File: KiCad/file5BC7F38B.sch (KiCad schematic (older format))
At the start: 72 parts, among them J301 DB9_Female, P301 ISP/PDI, P302 Thru, P304 Header, Q301 PN2222A, SW301 SPST, U301 DS3231, U302 ATmega1284P-AU, U303 LP2992, U304 SI5351A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

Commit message: Design Updates
Updating schematic parts
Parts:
- C303, C304, C313, C314, C315, C317, C318: footprint Capacitors_SMD:C_0805_HandSoldering -> Capacitors_SMD:C_0805
- R308, R313: footprint Resistors_SMD:R_0805_HandSoldering -> Resistors_SMD:R_0805
- SJ301: footprint (none) -> Wire_Connections_Bridges:Solder-Jumper-NO-SMD-Pad_Small; Digi-Key Part No. (none) -> np; Link (none) -> np; Manufacturer (none) -> np
- TP301: footprint (none) -> Pin_Headers:Pin_Header_Straight_1x03
- TP302: footprint (none) -> Pin_Headers:Pin_Header_Straight_1x04
- U304: footprint Housings_SSOP:MSOP-10_3x3mm_Pitch0.5mm_Handsolder -> Housings_SSOP:MSOP-10_3x3mm_Pitch0.5mm
- U307: footprint Housings_SSOP:TSSOP-8_3x3mm_Pitch0.65mm_Handsolder -> Housings_SSOP:TSSOP-8_3x3mm_Pitch0.65mm
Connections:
- net labels removed: CLK0, CLK2, PB5
- wire segments 298 -> 297
- no-connect marks 16 -> 19
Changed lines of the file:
@@
 F 0 "U304" H 11850 3650 60  0000 C CNB
 F 1 "SI5351A" H 11850 3150 60  0000 C CNB
-F 2 "Housings_SSOP:MSOP-10_3x3mm_Pitch0.5mm_Handsolder" H 11850 3150 50  0001 C CNN
+F 2 "Housings_SSOP:MSOP-10_3x3mm_Pitch0.5mm" H 11850 3150 50  0001 C CNN
 F 3 "http://www.silabs.com/Support%20Documents/TechnicalDocs/Si5351-B.pdf" H 11850 3150 50  0001 C CNN
 F 4 "336-2399-5-ND" H 11850 3150 50  0001 C CNN "Digi-Key Part No."
@@
 F 0 "C304" H 5500 4900 50  0000 L CNN
 F 1 "10uF" H 5550 5050 50  0000 L CNN
-F 2 "Capacitors_SMD:C_0805_HandSoldering" H 5450 5000 50  0001 C CNN
+F 2 "Capacitors_SMD:C_0805" H 5450 5000 50  0001 C CNN
 F 3 "" H 5450 5000 50  0001 C CNN
 F 4 "490-5523-1-ND" H 5450 5000 50  0001 C CNN "Digi-Key Part No."
@@
 	-1   0    0    1
 $EndComp
-Text Label 4350 5600 0    39   ~ 0
-PB3
-Text Label 3850 5500 2    39   ~ 0
-PB4
-Text Label 3850 5600 2    39   ~ 0
-PB5
 Text Notes 10750 2300 0    79   ~ 16
 SI5351 Clock
@@
 Connection ~ 10550 4350
 Wire Wire Line
-	12500 2250 12500 2950
-Wire Wire Line
 	12600 2250 12600 3050
 $Comp
@@
 Text GLabel 12600 2250 1    39   Output ~ 0
 CLK1
-Text GLabel 12500 2250 1    39   Output ~ 0
-CLK0
 Text GLabel 7950 6550 2    39   Output ~ 0
 HF_ENABLE
@@
 F 0 "U307" H 10200 4500 61  0000 C CNB
 F 1 "SN74CB3Q3305" H 10450 4000 61  0000 C CNB
-F 2 "Housings_SSOP:TSSOP-8_3x3mm_Pitch0.65mm_Handsolder" H 10050 3850 50  0001 C CNN
+F 2 "Housings_SSOP:TSSOP-8_3x3mm_Pitch0.65mm" H 10050 3850 50  0001 C CNN
 F 3 "" H 10050 4300 50  0001 C CNN
 F 4 "296-16809-1-ND" H 10050 4250 50  0001 C CNN "Digi-Key Part No."
@@
 	8250 3650 8250 3700
 Connection ~ 8250 3700
-Text GLabel 12500 3350 2    39   Output ~ 0
-CLK2
 Wire Wire Line
 	4450 3500 4450 3850
@@
 F 0 "TP302" V 9550 3650 50  0000 L CNN
 F 1 "I2C0" V 9450 3650 50  0000 L CNN
-F 2 "" H 9350 3800 50  0001 C CNN
+F 2 "Pin_Headers:Pin_Header_Straight_1x04" H 9350 3800 50  0001 C CNN
 F 3 "" H 9350 3800 50  0001 C CNN
 F 4 "np" H 9350 3800 50  0001 C CNN "Digi-Key Part No."
@@
 F 0 "TP301" V 10750 3700 50  0000 L CNN
 F 1 "I2C1" V 10650 3700 50  0000 L CNN
-F 2 "" H 10550 3800 50  0001 C CNN
+F 2 "Pin_Headers:Pin_Header_Straight_1x03" H 10550 3800 50  0001 C CNN
 F 3 "" H 10550 3800 50  0001 C CNN
 F 4 "np" H 10550 3800 50  0001 C CNN "Digi-Key Part No."
@@
 F 0 "R313" V 2630 9700 50  0000 C CNN
 F 1 "100k" V 2550 9700 50  0000 C CNN
-F 2 "Resistors_SMD:R_0805_HandSoldering" H 2480 9700 50  0001 C CNN
+F 2 "Resistors_SMD:R_0805" H 2480 9700 50  0001 C CNN
 F 3 "" H 2550 9700 50  0001 C CNN
 F 4 "311-100KCRCT-ND" H 2550 9700 50  0001 C CNN "Digi-Key Part No."
@@
 F 0 "SJ301" H 2950 7100 50  0000 C CNN
 F 1 "SolderJumper_2_Open" H 2950 7114 50  0001 C CNN
-F 2 "" H 2950 7000 50  0001 C CNN
+F 2 "Wire_Connections_Bridges:Solder-Jumper-NO-SMD-Pad_Small" H 2950 7000 50  0001 C CNN
 F 3 "" H 2950 7000 50  0001 C CNN
+F 4 "np" H 2950 7000 50  0001 C CNN "Digi-Key Part No."
+F 5 "np" H 2950 7000 50  0001 C CNN "Link"
+F 6 "np" H 2950 7000 50  0001 C CNN "Manufacturer"
 	1    2950 7000
 	0    -1   -1   0
@@
 F 0 "C303" H 2200 2150 50  0000 L CNN
 F 1 "4.7uF" H 2475 2150 50  0000 L CNN
-F 2 "Capacitors_SMD:C_0805_HandSoldering" H 2488 2100 50  0001 C CNN
+F 2 "Capacitors_SMD:C_0805" H 2488 2100 50  0001 C CNN
 F 3 "" H 2450 2250 50  0001 C CNN
 F 4 "587-2990-1-ND" H 2450 2250 50  0001 C CNN "Digi-Key Part No."
@@
 F 8 "IC REG LINEAR 3.3V 250MA SOT23-5" H 14750 6800 50  0001 C CNN "Description"
 	1    14750 6800
-	1    0    0    -1
+	-1   0    0    -1
 $EndComp
 $Comp
@@
 F 0 "C318" H 3650 2150 50  0000 L CNN
 F 1 "4.7uF" H 3925 2150 50  0000 L CNN
-F 2 "Capacitors_SMD:C_0805_HandSoldering" H 3938 2100 50  0001 C CNN
+F 2 "Capacitors_SMD:C_0805" H 3938 2100 50  0001 C CNN
 F 3 "" H 3900 2250 50  0001 C CNN
 F 4 "587-2990-1-ND" H 3900 2250 50  0001 C CNN "Digi-Key Part No."
@@
 F 0 "C317" H 3650 3550 50  0000 L CNN
 F 1 "4.7uF" H 3925 3550 50  0000 L CNN
-F 2 "Capacitors_SMD:C_0805_HandSoldering" H 3938 3500 50  0001 C CNN
+F 2 "Capacitors_SMD:C_0805" H 3938 3500 50  0001 C CNN
 F 3 "" H 3900 3650 50  0001 C CNN
 F 4 "587-2990-1-ND" H 3900 3650 50  0001 C CNN "Digi-Key Part No."
@@
 F 0 "C314" H 2200 3550 50  0000 L CNN
 F 1 "4.7uF" H 2475 3550 50  0000 L CNN
-F 2 "Capacitors_SMD:C_0805_HandSoldering" H 2488 3500 50  0001 C CNN
+F 2 "Capacitors_SMD:C_0805" H 2488 3500 50  0001 C CNN
 F 3 "" H 2450 3650 50  0001 C CNN
 F 4 "587-2990-1-ND" H 2450 3650 50  0001 C CNN "Digi-Key Part No."
@@
 F 0 "C313" H 13750 6850 50  0000 L CNN
 F 1 "4.7uF" H 14025 6850 50  0000 L CNN
-F 2 "Capacitors_SMD:C_0805_HandSoldering" H 14038 6800 50  0001 C CNN
+F 2 "Capacitors_SMD:C_0805" H 14038 6800 50  0001 C CNN
 F 3 "" H 14000 6950 50  0001 C CNN
 F 4 "587-2990-1-ND" H 14000 6950 50  0001 C CNN "Digi-Key Part No."
@@
 F 0 "C315" H 15200 6850 50  0000 L CNN
 F 1 "4.7uF" H 15475 6850 50  0000 L CNN
-F 2 "Capacitors_SMD:C_0805_HandSoldering" H 15488 6800 50  0001 C CNN
+F 2 "Capacitors_SMD:C_0805" H 15488 6800 50  0001 C CNN
 F 3 "" H 15450 6950 50  0001 C CNN
 F 4 "587-2990-1-ND" H 15450 6950 50  0001 C CNN "Digi-Key Part No."
@@
 F 0 "R308" V 2530 7400 50  0000 C CNN
 F 1 "100k" V 2450 7400 50  0000 C CNN
-F 2 "Resistors_SMD:R_0805_HandSoldering" H 2380 7400 50  0001 C CNN
+F 2 "Resistors_SMD:R_0805" H 2380 7400 50  0001 C CNN
 F 3 "" H 2450 7400 50  0001 C CNN
 F 4 "311-100KCRCT-ND" H 2450 7400 50  0001 C CNN "Digi-Key Part No."
@@
 	1    0    0    -1
 $EndComp
+Text Label 7800 3450 0    39   ~ 0
+PA0
+Text Label 7800 3550 0    39   ~ 0
+PA1
+NoConn ~ 12500 2950
+NoConn ~ 12500 3350
+NoConn ~ 8250 6750
 Wire Bus Line
 	7700 3250 7700 7050

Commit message: Design Updates
Updated schematics parts descriptions
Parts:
- D306, D307: symbol Diode:ESD9B5.0ST5G -> Power_Protection:TVS_Diode
- P301: symbol FlexFox80-rescue:CONN_02X03-ARDF-2-Band-MiniTx-rescue -> Connector:ISP_PDI
- U303, U306, U308: symbol FlexFox80-rescue:MIC5219-ARDF-2-Band-MiniTx-rescue -> Regulator_Linear:LP2992
- U307: symbol FlexFox80-rescue:SN74CB3Q3305-ARDF-2-Band-MiniTx-rescue -> Interface:SN74CB3Q3305
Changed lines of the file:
@@
 ~RESET~
 $Comp
-L FlexFox80-rescue:CONN_02X03-ARDF-2-Band-MiniTx-rescue P301
+L Connector:ISP_PDI P301
 U 1 1 57AD5B1A
 P 4100 5600
@@
 F 1 "ISP/PDI" H 4100 5400 50  0000 C CNN
 F 2 "Pin_Headers:SM_Pin_Header_Straight_2x03" H 4100 4400 50  0001 C CNN
-F 3 "http://katalog.we-online.de/em/datasheet/6100xx21121.pdf" H 4100 4400 50  0001 C CNN
+F 3 "" H 4100 4400 50  0001 C CNN
 F 4 "609-3487-1-ND" H 4100 5600 50  0001 C CNN "Digi-Key Part No."
 F 5 "<a href=\"https://www.digikey.com/products/en?keywords=609-3487-1-ND\">Link</a>" H 4100 5600 60  0001 C CNN "Link"
@@
 Connection ~ 10050 3900
 $Comp
-L FlexFox80-rescue:SN74CB3Q3305-ARDF-2-Band-MiniTx-rescue U307
+L Interface:SN74CB3Q3305 U307
 U 1 1 5C75D7C5
 P 10050 4250
@@
 	4200 2050 3900 2050
 $Comp
-L FlexFox80-rescue:MIC5219-ARDF-2-Band-MiniTx-rescue U303
+L Regulator_Linear:LP2992 U303
 U 1 1 60F38BB8
 P 3150 2100
@@
 	1000 8650 1700 8650
 $Comp
-L Diode:ESD9B5.0ST5G D306
+L Power_Protection:TVS_Diode D306
 U 1 1 612F5B15
 P 3750 9800
@@
 $EndComp
 $Comp
-L FlexFox80-rescue:MIC5219-ARDF-2-Band-MiniTx-rescue U308
+L Regulator_Linear:LP2992 U308
 U 1 1 60E1E02E
 P 3200 3550
@@
 $EndComp
 $Comp
-L FlexFox80-rescue:MIC5219-ARDF-2-Band-MiniTx-rescue U306
+L Regulator_Linear:LP2992 U306
 U 1 1 60E3CCEB
 P 14750 6800
@@
 $EndComp
 $Comp
-L Diode:ESD9B5.0ST5G D307
+L Power_Protection:TVS_Diode D307
 U 1 1 609FB9B8
 P 4100 9800

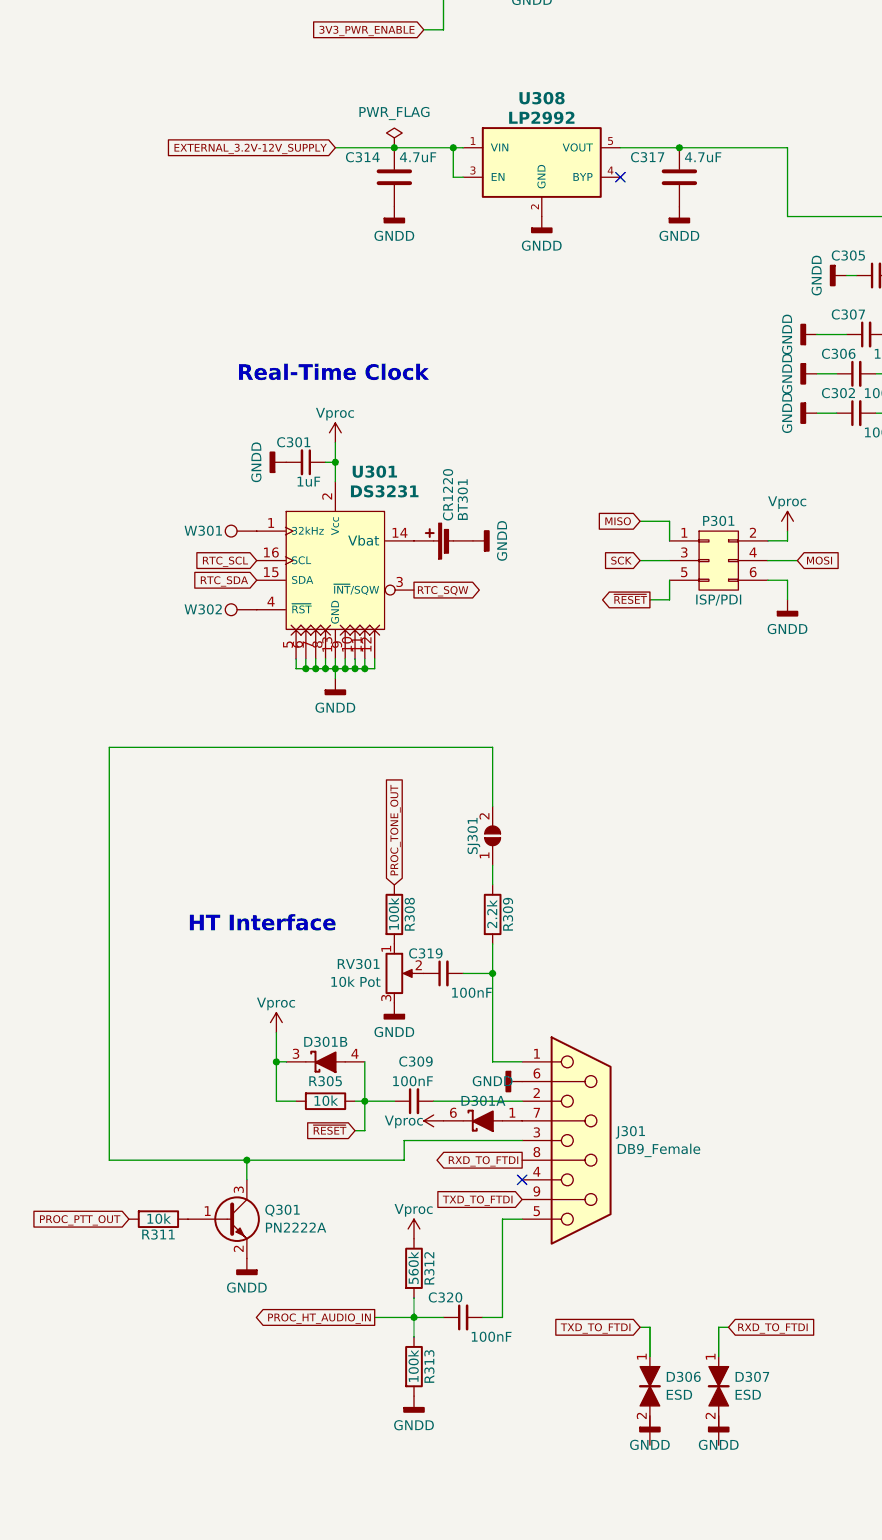
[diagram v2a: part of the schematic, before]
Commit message: PCB Updates
o Started PCB layout
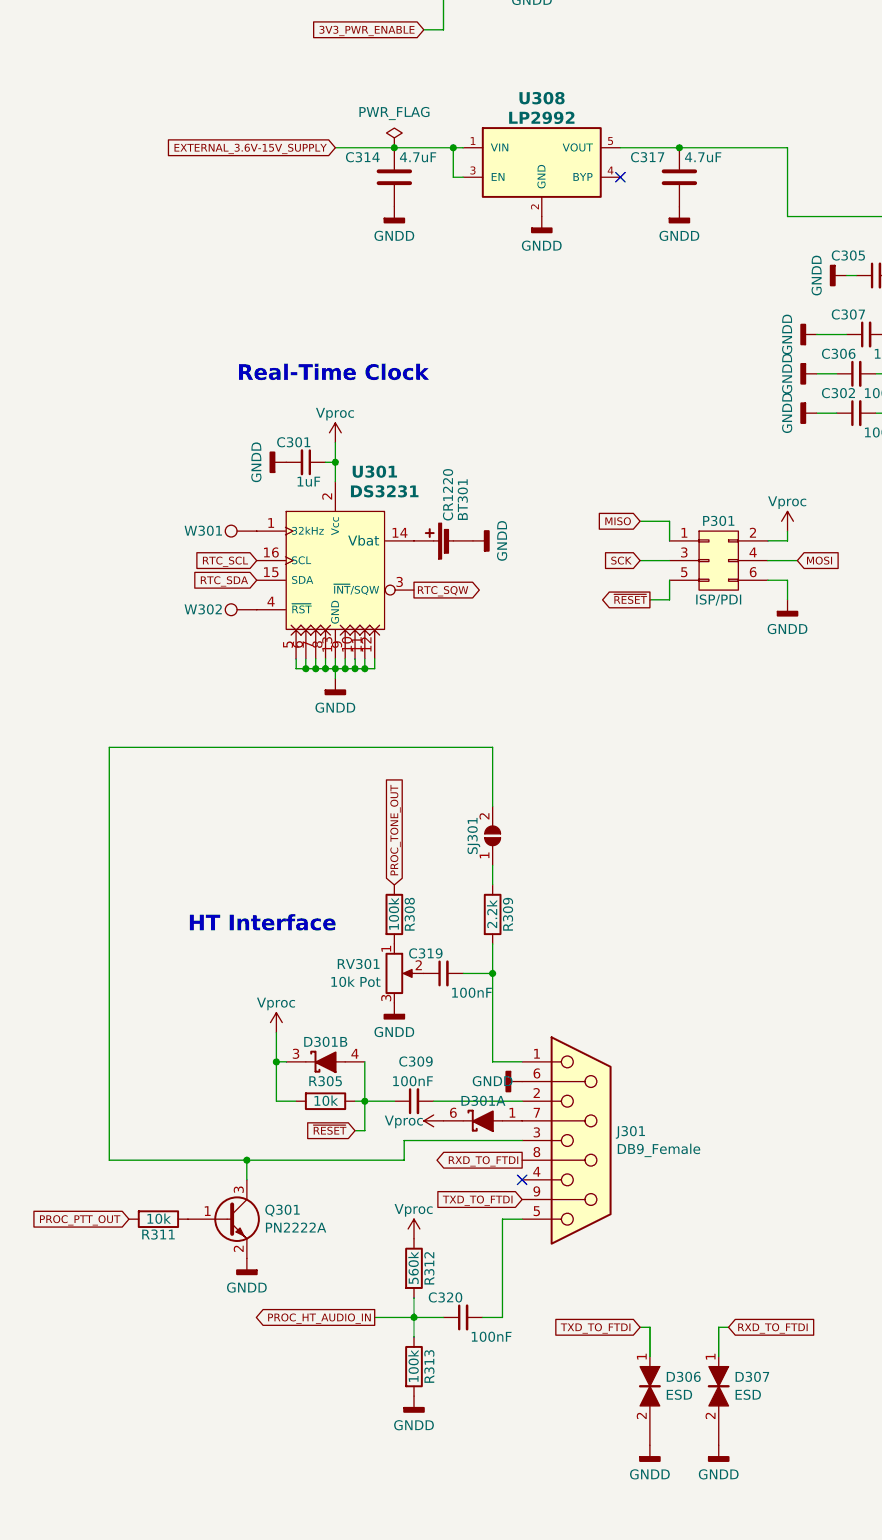
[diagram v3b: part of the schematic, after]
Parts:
- U302: footprint Package_QFP:TQFP-44_10x10mm_P0.8mm -> Housings_QFP:TQFP-44_10x10mm_Pitch0.8mm
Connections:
- net GND: now also D306.2, D307.2
- net EXTERNAL_3.2V-12V_SUPPLY renamed EXTERNAL_3.6V-15V_SUPPLY
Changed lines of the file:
@@
 Connection ~ 2750 3500
 Text GLabel 2150 3500 0    39   Input ~ 0
-EXTERNAL_3.2V-12V_SUPPLY
+EXTERNAL_3.6V-15V_SUPPLY
 NoConn ~ 3600 3650
 NoConn ~ 14350 6900
@@
 F 0 "U302" H 6550 7400 60  0000 C CNB
 F 1 "ATmega1284P-AU" H 6600 7250 60  0000 C CNB
-F 2 "Package_QFP:TQFP-44_10x10mm_P0.8mm" H 6550 5150 50  0001 C CIN
+F 2 "Housings_QFP:TQFP-44_10x10mm_Pitch0.8mm" H 6550 5150 50  0001 C CIN
 F 3 "http://ww1.microchip.com/downloads/en/DeviceDoc/Atmel-8272-8-bit-AVR-microcontroller-ATmega164A_PA-324A_PA-644A_PA-1284_P_datasheet.pdf" H 6550 5150 50  0001 C CNN
 F 4 "ATMEGA1284P-AU-ND" H 6550 5150 50  0001 C CNN "Digi-Key Part No."
@@
 L power:GNDD #PWR0213
 U 1 1 612F8482
-P 3750 9950
-F 0 "#PWR0213" H 3750 9700 50  0001 C CNN
-F 1 "GNDD" H 3750 9800 50  0000 C CNN
-F 2 "" H 3750 9950 50  0000 C CNN
-F 3 "" H 3750 9950 50  0000 C CNN
-	1    3750 9950
+P 3750 10100
+F 0 "#PWR0213" H 3750 9850 50  0001 C CNN
+F 1 "GNDD" H 3750 9950 50  0000 C CNN
+F 2 "" H 3750 10100 50  0000 C CNN
+F 3 "" H 3750 10100 50  0000 C CNN
+	1    3750 10100
 	1    0    0    -1
 $EndComp
@@
 L power:GNDD #PWR0214
 U 1 1 61314FDD
-P 4100 9950
-F 0 "#PWR0214" H 4100 9700 50  0001 C CNN
-F 1 "GNDD" H 4100 9800 50  0000 C CNN
-F 2 "" H 4100 9950 50  0000 C CNN
-F 3 "" H 4100 9950 50  0000 C CNN
-	1    4100 9950
-	1    0    0    -1
-$EndComp
+P 4100 10100
+F 0 "#PWR0214" H 4100 9850 50  0001 C CNN
+F 1 "GNDD" H 4100 9950 50  0000 C CNN
+F 2 "" H 4100 10100 50  0000 C CNN
+F 3 "" H 4100 10100 50  0000 C CNN
+	1    4100 10100
+	1    0    0    -1
+$EndComp

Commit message: PCB Updates
Layout work
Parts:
- added J302: Conn_01x06, Pin_Headers:Pin_Header_Angled_1x06, symbol Connector_Generic:Conn_01x06
- added J303: DB9_Male, Connect:DB9F_CI, symbol Connector:DB9_Male
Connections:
- new net: J302.6 (Pin_6), J303.2
- new net: J302.3 (Pin_3), J303.7
- new net: J302.4 (Pin_4), J303.8
- new net: J302.5 (Pin_5), J303.9
- new net GND1: J302.1 (Pin_1), J302.2 (Pin_2), J303.6
- no-connect marks 19 -> 23
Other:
- note added: "FTDI PROGRAMMING ADAPTER"
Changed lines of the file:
@@
 U 1 1 619A55E4
 P 3400 8550
-F 0 "J301" H 3580 8596 50  0000 L CNN
-F 1 "DB9_Female" H 3580 8505 50  0000 L CNN
+F 0 "J301" H 3250 9250 50  0000 L CNN
+F 1 "DB9_Female" H 3250 9150 50  0000 L CNN
 F 2 "Connect:DB9F_CI" H 3400 8550 50  0001 C CNN
 F 3 "" H 3400 8550 50  0001 C CNN
@@
 NoConn ~ 12500 3350
 NoConn ~ 8250 6750
+$Comp
+L Connector:DB9_Male J303
+U 1 1 609FE9A1
+P 4800 8550
+F 0 "J303" H 4718 7858 50  0000 C CNN
+F 1 "DB9_Male" H 4718 7949 50  0000 C CNN
+F 2 "Connect:DB9F_CI" H 4800 8550 50  0001 C CNN
+F 3 "" H 4800 8550 50  0001 C CNN
+F 4 "609-5908-ND" H 4800 8550 50  0001 C CNN "Digi-Key Part No."
+F 5 "<a href=\"https://www.digikey.com/products/en?keywords=609-5908-ND\">Link</a>" H 4800 8550 50  0001 C CNN "Link"
+F 6 "Amphenol ICC (FCI)" H 4800 8550 50  0001 C CNN "Manufacturer"
+F 7 "DE09P065TXLF" H 4800 8550 50  0001 C CNN "Manufacturer PN"
+F 8 "9 Position D-Sub Plug, Male Pins Connector" H 4800 8550 50  0001 C CNN "Description"
+	1    4800 8550
+	-1   0    0    1
+$EndComp
+$Comp
+L Connector_Generic:Conn_01x06 J302
+U 1 1 60A04D07
+P 5600 8500
+F 0 "J302" H 5680 8492 50  0000 L CNN
+F 1 "Conn_01x06" H 5680 8401 50  0000 L CNN
+F 2 "Pin_Headers:Pin_Header_Angled_1x06" H 5600 8500 50  0001 C CNN
+F 3 "" H 5600 8500 50  0001 C CNN
+F 4 "929550-01-06-ND" H 5600 8500 50  0001 C CNN "Digi-Key Part No."
+F 5 "<a href=\"https://www.digikey.com/products/en?keywords=929550-01-06-ND\">Link</a>" H 5600 8500 50  0001 C CNN "Link"
+F 6 "TH" H 5600 8500 50  0001 C CNN "Manufacturer"
+F 7 "TH" H 5600 8500 50  0001 C CNN "Manufacturer PN"
+	1    5600 8500
+	1    0    0    -1
+$EndComp
+NoConn ~ 5100 8950
+NoConn ~ 5100 8750
+NoConn ~ 5100 8550
+NoConn ~ 5100 8150
+Wire Wire Line
+	5400 8300 5350 8300
+Wire Wire Line
+	5400 8400 5350 8400
+Wire Wire Line
+	5350 8400 5350 8300
+Wire Wire Line
+	5400 8500 5200 8500
+Wire Wire Line
+	5200 8500 5200 8450
+Wire Wire Line
+	5200 8450 5100 8450
+Wire Wire Line
+	5400 8600 5200 8600
+Wire Wire Line
+	5200 8600 5200 8650
+Wire Wire Line
+	5200 8650 5100 8650
+Wire Wire Line
+	5400 8700 5200 8700
+Wire Wire Line
+	5200 8700 5200 8850
+Wire Wire Line
+	5200 8850 5100 8850
+Wire Wire Line
+	5400 8800 5300 8800
+Wire Wire Line
+	5300 8800 5300 8350
+Wire Wire Line
+	5300 8350 5100 8350
+Wire Wire Line
+	5100 8250 5350 8250
+Wire Wire Line
+	5350 8250 5350 8300
+Connection ~ 5350 8300
+Wire Notes Line
+	4500 7750 4500 9200
+Wire Notes Line
+	4500 9200 6150 9200
+Wire Notes Line
+	6150 9200 6150 7750
+Wire Notes Line
+	6150 7750 4500 7750
+Text Notes 4650 7700 0    61   ~ 12
+FTDI PROGRAMMING ADAPTER
 Wire Bus Line
 	7700 3250 7700 7050
+$Comp
+L power:GND1 #PWR?
+U 1 1 60CAA620
+P 5350 8250
+F 0 "#PWR?" H 5350 8000 50  0001 C CNN
+F 1 "GND1" H 5355 8077 50  0000 C CNN
+F 2 "" H 5350 8250 50  0001 C CNN
+F 3 "" H 5350 8250 50  0001 C CNN
+	1    5350 8250
+	1    0    0    1
+$EndComp
+Connection ~ 5350 8250
 $EndSCHEMATC

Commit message: BOM Updates
Corrections to part information in schematic and BOMs
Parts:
- D301: value MBD54DWT1GOSCT-ND -> MBD54
- R308, R313: Description RES SMD 10K OHM 1% 1/8W 0805 -> RES SMD 100K OHM 1% 1/8W 0805
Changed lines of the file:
@@
 F 6 "Yageo" H 2550 9700 50  0001 C CNN "Manufacturer"
 F 7 "RC0805FR-07100KL" H 2550 9700 50  0001 C CNN "Manufacturer PN"
-F 8 "RES SMD 10K OHM 1% 1/8W 0805" H 2550 9700 50  0001 C CNN "Description"
+F 8 "RES SMD 100K OHM 1% 1/8W 0805" H 2550 9700 50  0001 C CNN "Description"
 	1    2550 9700
 	1    0    0    -1
@@
 P 2900 8450
 F 0 "D301" H 2900 8350 50  0000 C CNN
-F 1 "MBD54DWT1GOSCT-ND" H 2925 8725 50  0001 C CNN
+F 1 "MBD54" H 2925 8725 50  0001 C CNN
 F 2 "TO_SOT_Packages_SMD:SOT-363-0.65" H 2900 8450 50  0001 C CNN
 F 3 "" H 2900 8450 50  0001 C CNN
@@
 P 2100 8150
 F 0 "D301" H 2100 8050 50  0000 C CNN
-F 1 "MBD54DWT1GOSCT-ND" H 2125 8425 50  0001 C CNN
+F 1 "MBD54" H 2125 8425 50  0001 C CNN
 F 2 "TO_SOT_Packages_SMD:SOT-363-0.65" H 2100 8150 50  0001 C CNN
 F 3 "" H 2100 8150 50  0001 C CNN
@@
 F 6 "Yageo" H 2450 7400 50  0001 C CNN "Manufacturer"
 F 7 "RC0805FR-07100KL" H 2450 7400 50  0001 C CNN "Manufacturer PN"
-F 8 "RES SMD 10K OHM 1% 1/8W 0805" H 2450 7400 50  0001 C CNN "Description"
+F 8 "RES SMD 100K OHM 1% 1/8W 0805" H 2450 7400 50  0001 C CNN "Description"
 	1    2450 7400
 	1    0    0    -1
